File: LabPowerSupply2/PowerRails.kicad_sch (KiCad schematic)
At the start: 8 parts

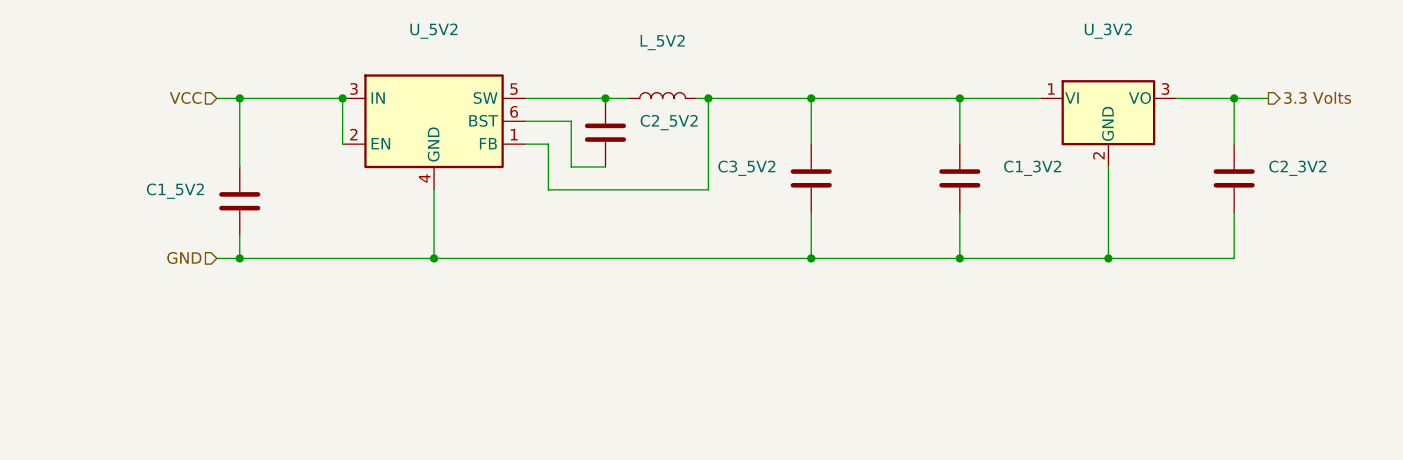
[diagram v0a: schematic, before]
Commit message: Changed symbols to actual MOSFETs
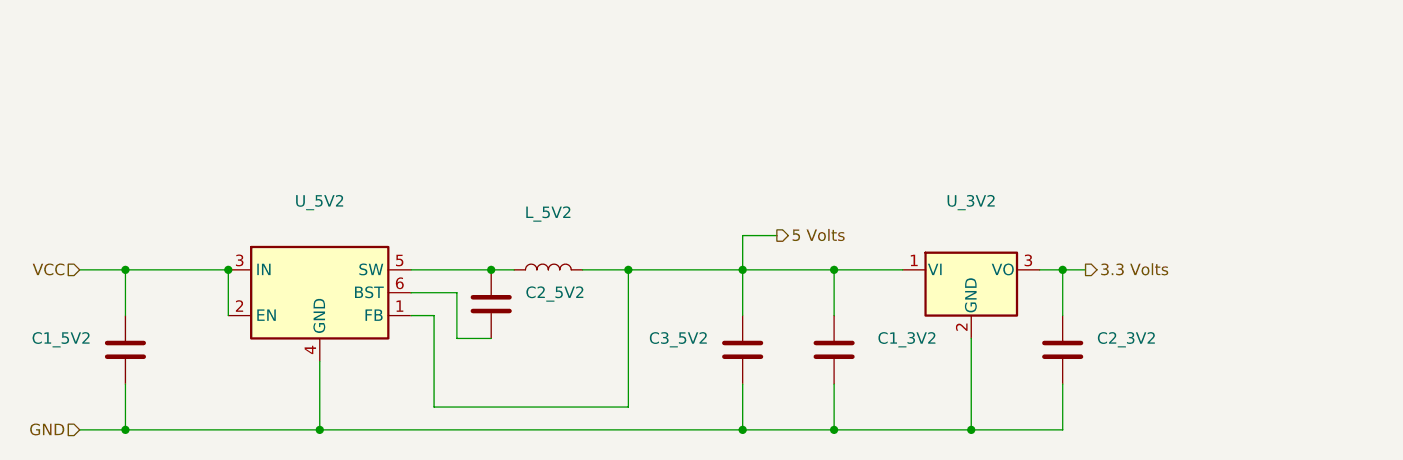
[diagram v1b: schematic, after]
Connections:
- net 5 Volts: now reaches C1_3V2.2, C3_5V2.2, L_5V2.2, U_3V2.1 (VI), U_5V2.1 (FB)
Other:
- title: Channel 2 3.3 Volt Power Rail -> Channel 1 Power Rails

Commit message: Added plots for voltage and current error along with their data and scripts
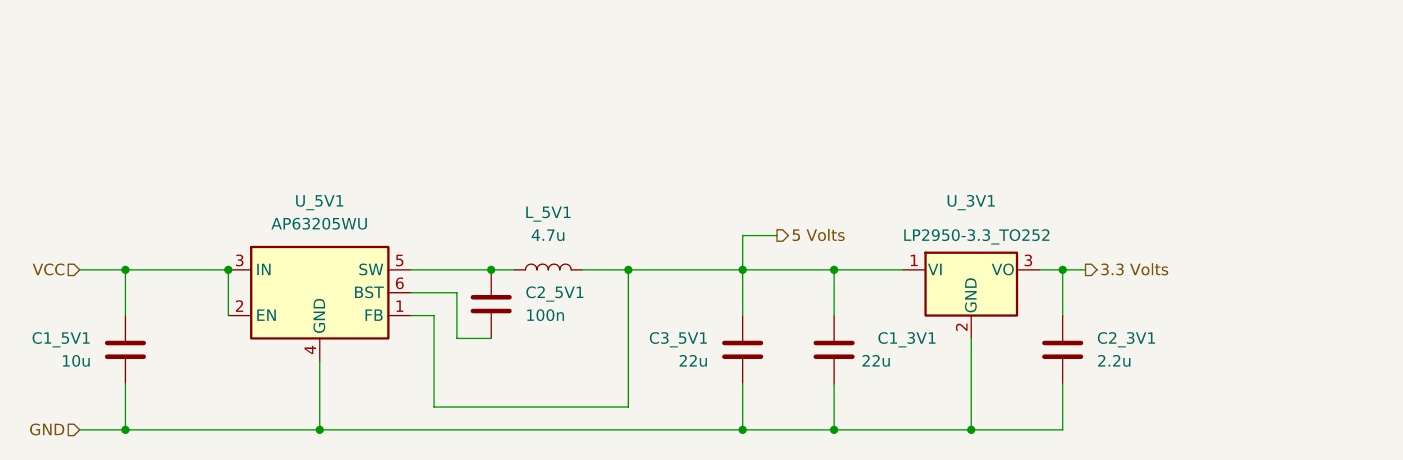
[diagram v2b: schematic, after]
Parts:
- C1_3V1: renamed from C1_3V2; value (none) -> 22u; footprint (none) -> Capacitor_SMD:C_1210_3225Metric
- C1_5V1: renamed from C1_5V2; value (none) -> 10u; footprint (none) -> Capacitor_SMD:C_1206_3216Metric
- C2_3V1: renamed from C2_3V2; value (none) -> 2.2u; footprint (none) -> Capacitor_SMD:C_0805_2012Metric
- C2_5V1: renamed from C2_5V2; value (none) -> 100n; footprint (none) -> Capacitor_SMD:C_0603_1608Metric
- C3_5V1: renamed from C3_5V2; value (none) -> 22u; footprint (none) -> Capacitor_SMD:C_1210_3225Metric
- L_5V1: renamed from L_5V2; value (none) -> 4.7u; footprint (none) -> Inductor_SMD:L_Sumida_CDMC6D28_7.25x6.5mm
- U_3V1: renamed from U_3V2; value (none) -> LP2950-3.3_TO252; footprint (none) -> Package_TO_SOT_SMD:TO-252-2
- U_5V1: renamed from U_5V2; value (none) -> AP63205WU; footprint (none) -> Package_TO_SOT_SMD:TSOT-23-6
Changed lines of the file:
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@@
   (symbol (lib_id "Device:C") (at 181.61 97.79 0) (mirror x) (unit 1)
     (in_bom yes) (on_board yes)
-    (property "Reference" "C1_3V2" (id 0) (at 193.04 96.52 0)
+    (property "Reference" "C1_3V1" (id 0) (at 193.04 96.52 0)
       (effects (font (size 1.27 1.27)) (justify right))
     )
-    (property "Value" "" (id 1) (at 187.96 99.06 0)
+    (property "Value" "22u" (id 1) (at 187.96 99.06 0)
       (effects (font (size 1.27 1.27)) (justify right))
     )
-    (property "Footprint" "" (id 2) (at 182.5752 93.98 0)
+    (property "Footprint" "Capacitor_SMD:C_1210_3225Metric" (id 2) (at 182.5752 93.98 0)
       (effects (font (size 1.27 1.27)) hide)
     )
@@
   (symbol (lib_id "Device:C") (at 207.01 97.79 0) (unit 1)
     (in_bom yes) (on_board yes) (fields_autoplaced)
-    (property "Reference" "C2_3V2" (id 0) (at 210.82 96.5199 0)
+    (property "Reference" "C2_3V1" (id 0) (at 210.82 96.5199 0)
       (effects (font (size 1.27 1.27)) (justify left))
     )
-    (property "Value" "" (id 1) (at 210.82 99.0599 0)
+    (property "Value" "2.2u" (id 1) (at 210.82 99.0599 0)
       (effects (font (size 1.27 1.27)) (justify left))
     )
-    (property "Footprint" "" (id 2) (at 207.9752 101.6 0)
+    (property "Footprint" "Capacitor_SMD:C_0805_2012Metric" (id 2) (at 207.9752 101.6 0)
       (effects (font (size 1.27 1.27)) hide)
     )
@@
   (symbol (lib_id "Device:L") (at 149.86 88.9 90) (unit 1)
     (in_bom yes) (on_board yes) (fields_autoplaced)
-    (property "Reference" "L_5V2" (id 0) (at 149.86 82.55 90))
-    (property "Value" "" (id 1) (at 149.86 85.09 90))
-    (property "Footprint" "" (id 2) (at 149.86 88.9 0)
+    (property "Reference" "L_5V1" (id 0) (at 149.86 82.55 90))
+    (property "Value" "4.7u" (id 1) (at 149.86 85.09 90))
+    (property "Footprint" "Inductor_SMD:L_Sumida_CDMC6D28_7.25x6.5mm" (id 2) (at 149.86 88.9 0)
       (effects (font (size 1.27 1.27)) hide)
     )
@@
   (symbol (lib_id "Regulator_Linear:LP2950-3.3_TO252") (at 196.85 88.9 0) (unit 1)
     (in_bom yes) (on_board yes)
-    (property "Reference" "U_3V2" (id 0) (at 196.85 81.28 0))
-    (property "Value" "" (id 1) (at 189.23 85.09 0)
+    (property "Reference" "U_3V1" (id 0) (at 196.85 81.28 0))
+    (property "Value" "LP2950-3.3_TO252" (id 1) (at 189.23 85.09 0)
       (effects (font (size 1.27 1.27)) (justify left))
     )
-    (property "Footprint" "" (id 2) (at 196.85 83.185 0)
+    (property "Footprint" "Package_TO_SOT_SMD:TO-252-2" (id 2) (at 196.85 83.185 0)
       (effects (font (size 1.27 1.27) italic) hide)
     )
@@
   (symbol (lib_id "Device:C") (at 102.87 97.79 0) (mirror x) (unit 1)
     (in_bom yes) (on_board yes) (fields_autoplaced)
-    (property "Reference" "C1_5V2" (id 0) (at 99.06 96.5199 0)
+    (property "Reference" "C1_5V1" (id 0) (at 99.06 96.5199 0)
       (effects (font (size 1.27 1.27)) (justify right))
     )
-    (property "Value" "" (id 1) (at 99.06 99.0599 0)
+    (property "Value" "10u" (id 1) (at 99.06 99.0599 0)
       (effects (font (size 1.27 1.27)) (justify right))
     )
-    (property "Footprint" "" (id 2) (at 103.8352 93.98 0)
+    (property "Footprint" "Capacitor_SMD:C_1206_3216Metric" (id 2) (at 103.8352 93.98 0)
       (effects (font (size 1.27 1.27)) hide)
     )
@@
   (symbol (lib_id "Device:C") (at 171.45 97.79 0) (mirror x) (unit 1)
     (in_bom yes) (on_board yes) (fields_autoplaced)
-    (property "Reference" "C3_5V2" (id 0) (at 167.64 96.5199 0)
+    (property "Reference" "C3_5V1" (id 0) (at 167.64 96.5199 0)
       (effects (font (size 1.27 1.27)) (justify right))
     )
-    (property "Value" "" (id 1) (at 167.64 99.0599 0)
+    (property "Value" "22u" (id 1) (at 167.64 99.0599 0)
       (effects (font (size 1.27 1.27)) (justify right))
     )
-    (property "Footprint" "" (id 2) (at 172.4152 93.98 0)
+    (property "Footprint" "Capacitor_SMD:C_1210_3225Metric" (id 2) (at 172.4152 93.98 0)
       (effects (font (size 1.27 1.27)) hide)
     )
@@
   (symbol (lib_id "Device:C") (at 143.51 92.71 0) (unit 1)
     (in_bom yes) (on_board yes) (fields_autoplaced)
-    (property "Reference" "C2_5V2" (id 0) (at 147.32 91.4399 0)
+    (property "Reference" "C2_5V1" (id 0) (at 147.32 91.4399 0)
       (effects (font (size 1.27 1.27)) (justify left))
     )
-    (property "Value" "" (id 1) (at 147.32 93.9799 0)
+    (property "Value" "100n" (id 1) (at 147.32 93.9799 0)
       (effects (font (size 1.27 1.27)) (justify left))
     )
-    (property "Footprint" "" (id 2) (at 144.4752 96.52 0)
+    (property "Footprint" "Capacitor_SMD:C_0603_1608Metric" (id 2) (at 144.4752 96.52 0)
       (effects (font (size 1.27 1.27)) hide)
     )
@@
   (symbol (lib_id "Regulator_Switching:AP63205WU") (at 124.46 91.44 0) (unit 1)
     (in_bom yes) (on_board yes) (fields_autoplaced)
-    (property "Reference" "U_5V2" (id 0) (at 124.46 81.28 0))
-    (property "Value" "" (id 1) (at 124.46 83.82 0))
-    (property "Footprint" "" (id 2) (at 124.46 114.3 0)
+    (property "Reference" "U_5V1" (id 0) (at 124.46 81.28 0))
+    (property "Value" "AP63205WU" (id 1) (at 124.46 83.82 0))
+    (property "Footprint" "Package_TO_SOT_SMD:TSOT-23-6" (id 2) (at 124.46 114.3 0)
       (effects (font (size 1.27 1.27)) hide)
     )
